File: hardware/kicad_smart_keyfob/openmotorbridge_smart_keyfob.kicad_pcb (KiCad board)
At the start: 2 copper layers, 38 x 19 mm, 25 parts, among them M1 LRA_MOTOR_PADS, SW1 BTN_ARM, SW2 BTN_SOS, U1 nRF52840-QIAA, U2 SX1262IMLTRT, U3 DRV2605LDGSR, U4 BQ51003YFPR, U5 BQ25100YFPR, Y1 32.000MHz, Y2 32.768kHz, Y3 32MHz_TCXO

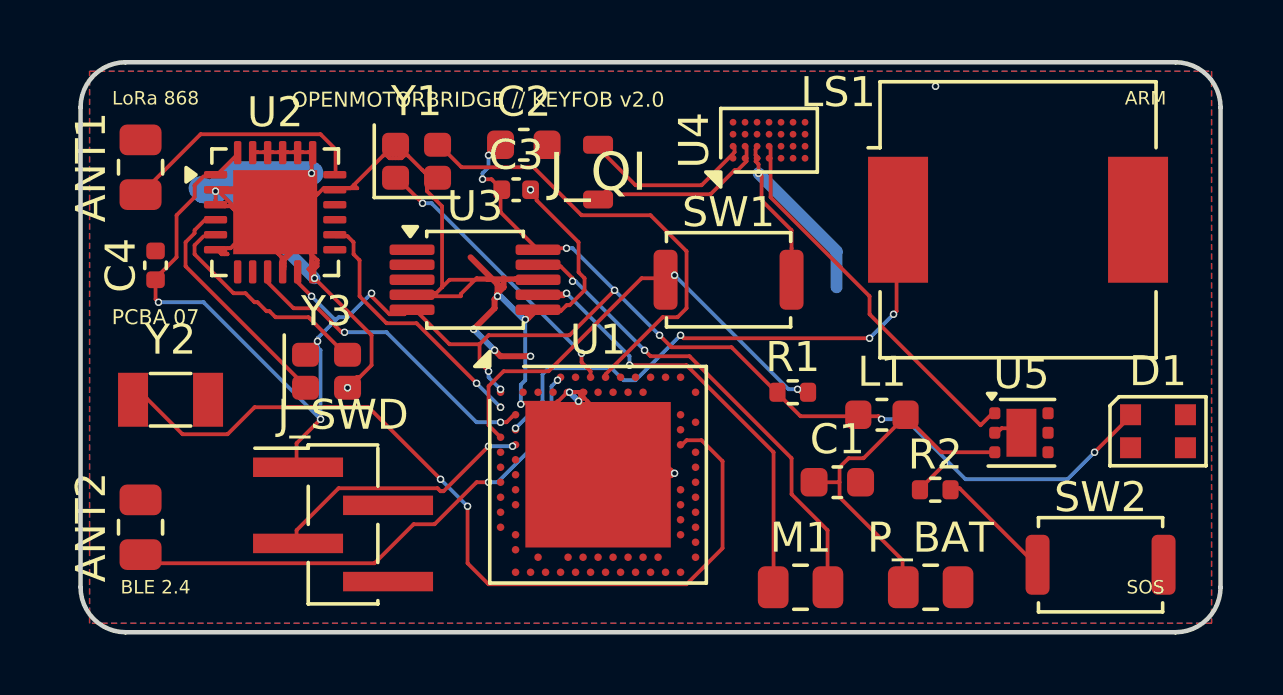
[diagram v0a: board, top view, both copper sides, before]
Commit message: fix(hardware): fleet-wide 7-PCBA remediation, schematic parity & doc alignment
- PCBA 01 (Central Box): Synchronized DTM-12 schematic and PCB routing, purged obsolete analog audio transformers/HD26 connector.
- PCBA 03 (Smart Cartridge): Verified Kelvin ground isolation on J_AUDIO_PWR, resolved U1.16 BAY_SELECT single net.
- PCBA 05 (Front Node): Mapped DW3110 UWB SPI/IRQ/RST to ESP32-S3 pads 30-35, connected MK1 I2S MEMS mic and Y_UWB crystal.
- PCBA 07 (Smart Keyfob): Connected 12 unrouted signals (SX1262 LoRa SPI, DRV2605L I2C, SWD, RTC crystal, buttons) to nRF52840 pads.
- PCBA 08 (Radar Sub-MCU): Synchronized J1.1 power rail to VCC_5V, connected Y1_UWB crystal to DW3110 pads 4 & 5.
- PCBA 09 & PCBA 10 (OMM 2.4 GHz & 446 MHz): Verified 4-layer stackup, BQ24075 ground ties, SA818 isolation, and vertical B.Cu J_HELMET orientation.
- Tools: Added verify_hardware_integrity.py with automated DRC/parity/single-net/floating-pad checks (all 7 PCBAs HEALTHY).
- Docs: Synchronized docs/de and docs/en hardware specifications, pinouts, and DTM-12 architecture.
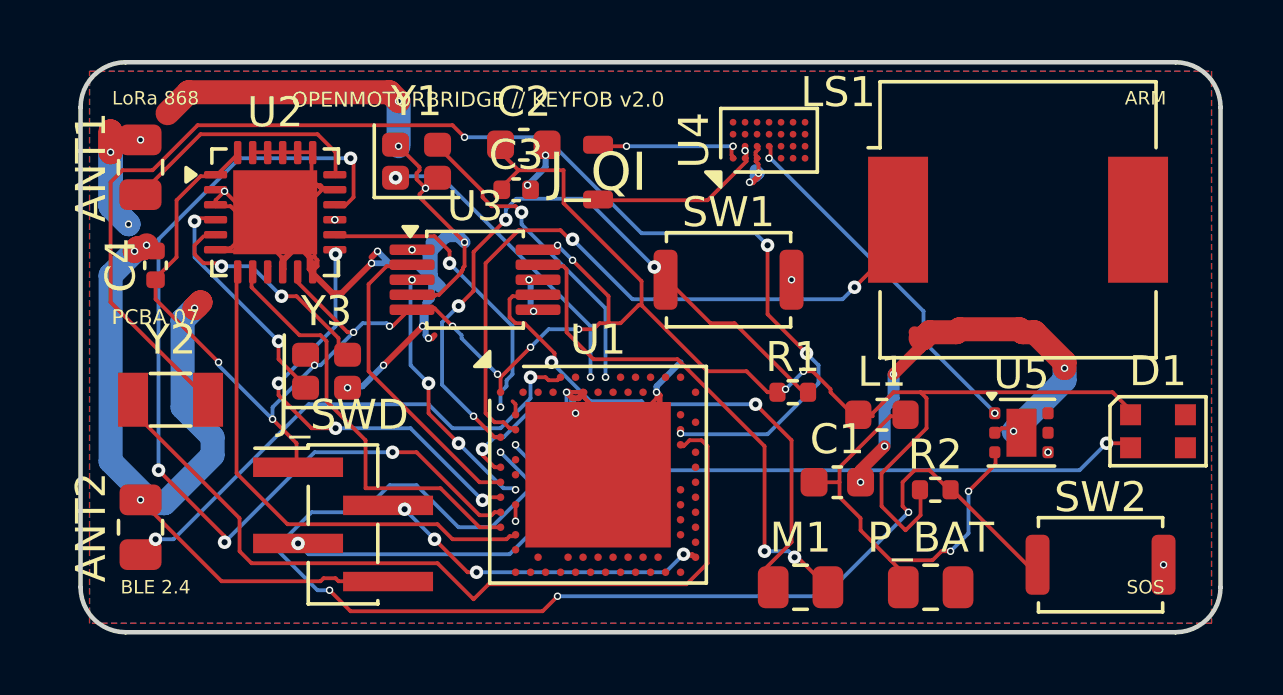
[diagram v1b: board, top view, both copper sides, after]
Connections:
- U1 pad AC24: (no net) -> SWDIO
- U1 pad F23: (no net) -> RTC1
- U1 pad J1: (no net) -> BTN_SOS_N
- U1 pad K2: (no net) -> CHG_STAT
- U1 pad L1: (no net) -> LED_DATA
- U1 pad M2: (no net) -> DRV_EN
- U1 pad N1: (no net) -> I2C_SDA
- U1 pad P2: (no net) -> I2C_SCL
- U1 pad R1: (no net) -> LORA_NSS
- U1 pad T2: (no net) -> LORA_MOSI
- U1 pad U1: (no net) -> LORA_MISO
- U1 pad W1: (no net) -> LORA_BUSY
- U1 pad Y2: (no net) -> LORA_RESET
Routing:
- net GND: track 73.1 -> 131.4 mm, vias 16 -> 34
- net RTC1: track 0.00 -> 43.7 mm, vias 0 -> 4
- net BTN_SOS_N: track 3.98 -> 42.6 mm, vias 0 -> 4
- net LORA_MISO: track 0.00 -> 32.0 mm, vias 0 -> 4
- net LED_DATA: track 0.00 -> 24.6 mm, vias 0 -> 2
- net LORA_RESET: track 0.00 -> 17.0 mm
- net LORA_NSS: track 0.00 -> 14.6 mm, vias 0 -> 4
- net LORA_BUSY: track 0.00 -> 14.3 mm
- net SWDIO: track 0.00 -> 11.9 mm, vias 0 -> 4
- net VCC_3V3: track 63.3 -> 74.3 mm, vias 15 -> 13
- net I2C_SDA: track 0.00 -> 10.6 mm
- net LORA_DIO1: track 10.3 -> 0.77 mm, vias 2 -> 0
- net I2C_SCL: track 0.00 -> 8.68 mm, vias 0 -> 4
- net BTN_ARM_N: track 15.3 -> 22.3 mm, vias 2 -> 4
- net XTAL2: track 15.3 -> 10.5 mm, vias 0 -> 2
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
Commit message: feat(hardware): achieve 100% 0-error DRC across all 7 official PCBAs and complete 4-layer Cartridge audio switching
- PCBA 01 (Central Box): Resolved keepout zone violation at U.FL ANT1, refilled zones (0 errors, 0 unconnected).
- PCBA 03 (Universal Smart Cartridge): Upgraded to 4 layers (JLC04161H), added SPDT analog/digital switch U4 (TS5A3159DBVR) on B.Cu and 10k pull-up R9 on F.Cu, routed symmetrical audio/OMM nets, schematic ERC 0 errors, DRC 0 errors, 0 unconnected.
- PCBA 05 (Front Node): 4-layer upgrade, solid GND plane, snapped OTTOCAST_FAULT_N (0 errors, 0 unconnected).
- PCBA 07 (Smart Keyfob): 4-layer upgrade, fixed Edge.Cuts arc alignment, routed U2 pad 23 (0 errors, 0 unconnected).
- PCBA 08 (Radar Sub-MCU), PCBA 09 (OMM 2.4 GHz), PCBA 10 (OMM 446 MHz): Verified 100% clean (0 errors, 0 unconnected).
- Added reproducibility tools: tools/sync_cartridge_sch.py and tools/remediate_pcba03.py.
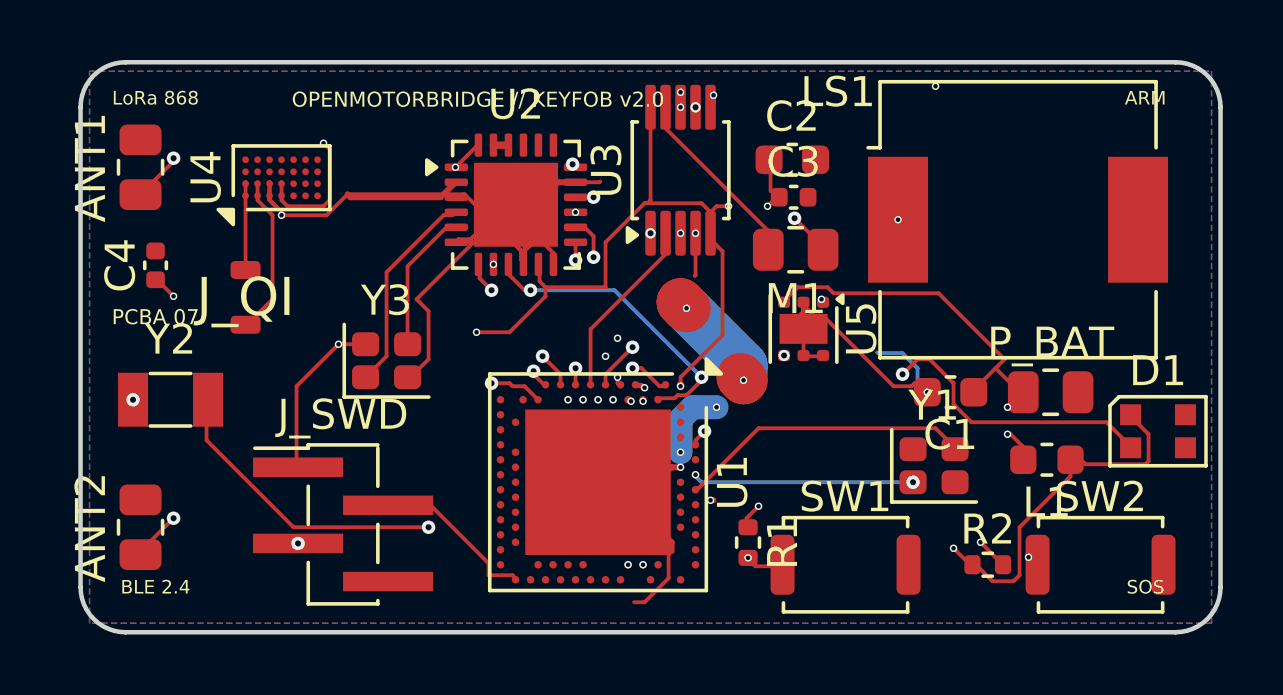
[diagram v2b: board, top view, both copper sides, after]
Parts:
- moved Y1 20.0 mm to (128.4, 83.5)
- moved U4 16.3 mm to (106.7, 73.8)
- moved J_QI 12.5 mm to (105.5, 77.8)
- moved M1 11.3 mm to (123.8, 76.2), turned to 180 degrees
- moved SW1 10.3 mm to (125.5, 86.8)
- moved C3 9.25 mm to (123.8, 74.5)
- moved C2 8.96 mm to (123.7, 73.2)
- moved U5 8.05 mm to (124.1, 78.9), turned to -90 degrees
- moved U2 8.03 mm to (114.5, 74.8)
- moved U3 7.76 mm to (120.0, 73.6), turned to 90 degrees
- moved P_BAT 7.63 mm to (132.3, 81.0)
- moved L1 5.70 mm to (132.2, 83.2), turned to 180 degrees
- moved R1 5.23 mm to (122.2, 86.0), turned to -90 degrees
- moved C1 4.82 mm to (129.0, 81.0), turned to 180 degrees
- moved R2 3.05 mm to (130.2, 86.8)
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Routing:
- net GND: track 131.4 -> 62.7 mm, vias 34 -> 13
- net RTC1: track 43.7 -> 17.8 mm, vias 4 -> 2
- net LORA_MISO: track 32.0 -> 8.25 mm, vias 4 -> 2
- net BTN_SOS_N: track 42.6 -> 22.8 mm, vias 4 -> 5
- net BTN_ARM_N: track 22.3 -> 9.04 mm, vias 4 -> 2
- net BUZZER_PWM: track 23.0 -> 11.0 mm
- net LRA_POS: track 18.5 -> 6.55 mm
- net VCC_QI_5V: track 12.1 -> 23.4 mm
- net LRA_NEG: track 17.5 -> 6.16 mm, vias 2 -> 0
- net LORA_RESET: track 17.0 -> 6.00 mm, vias 0 -> 2
- net LORA_NSS: track 14.6 -> 4.85 mm, vias 4 -> 2
- net RTC2: track 28.4 -> 18.7 mm, vias 0 -> 2
- net LORA_BUSY: track 14.3 -> 4.75 mm, vias 0 -> 2
- net LORA_DIO1: track 0.77 -> 10.2 mm, vias 0 -> 2
- net DRV_EN: track 0.00 -> 8.50 mm, vias 1 -> 2
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- added copper zone on In1.Cu, net GND
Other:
- copper layers 2 -> 4
